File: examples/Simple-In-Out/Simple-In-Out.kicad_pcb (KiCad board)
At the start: 2 copper layers, 2 parts, among them J1 IN, J2 OUT

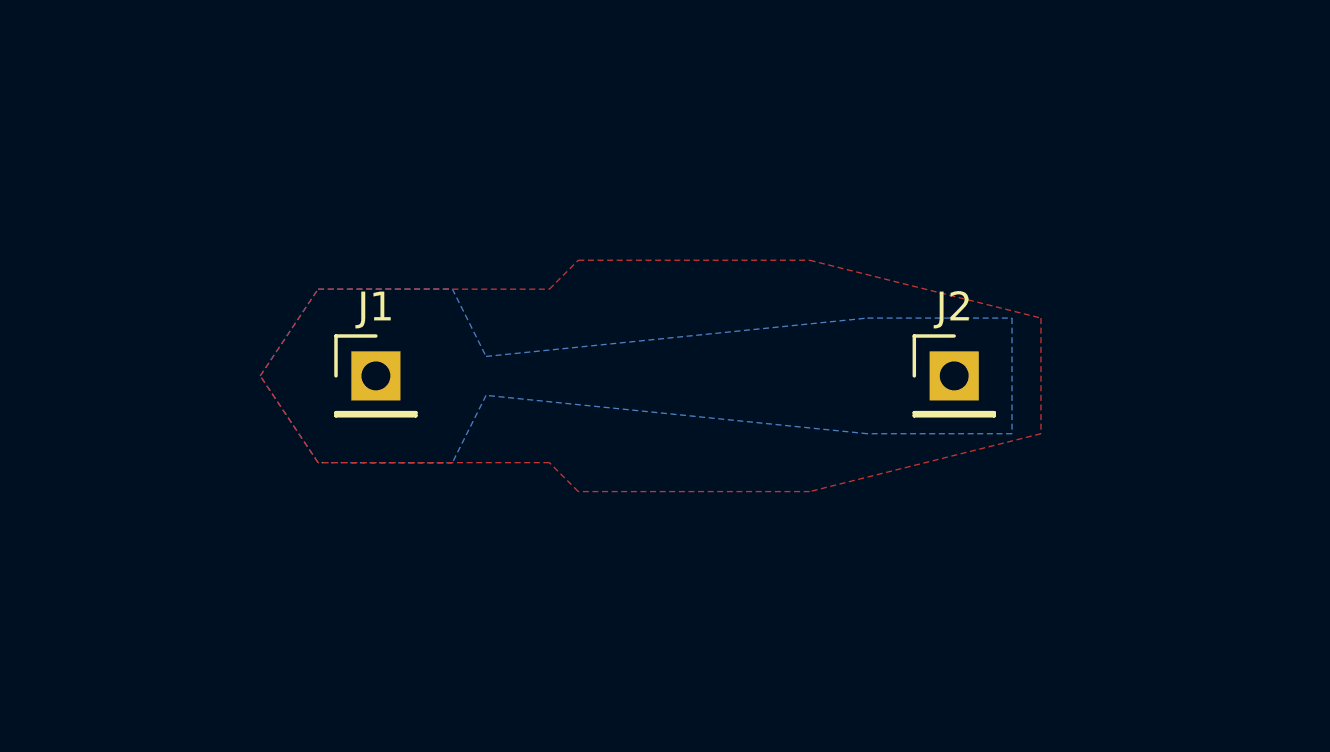
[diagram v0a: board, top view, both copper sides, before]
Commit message: Fix edge cuts
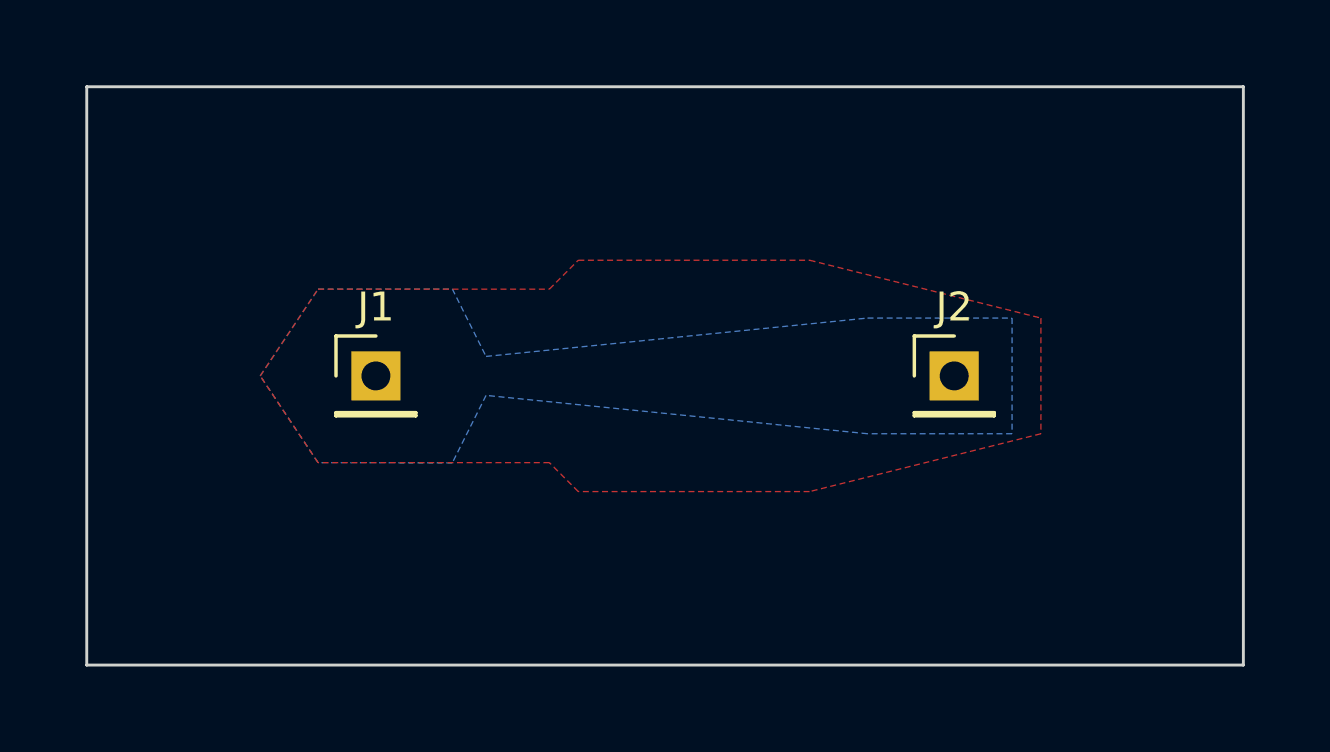
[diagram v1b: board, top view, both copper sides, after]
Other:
- board outline added: 40 x 20 mm
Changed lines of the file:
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@@
 		)
 		(fill no)
-		(layer "Eco2.User")
+		(layer "Edge.Cuts")
 	)
 	(zone

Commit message: Add GND net and vias
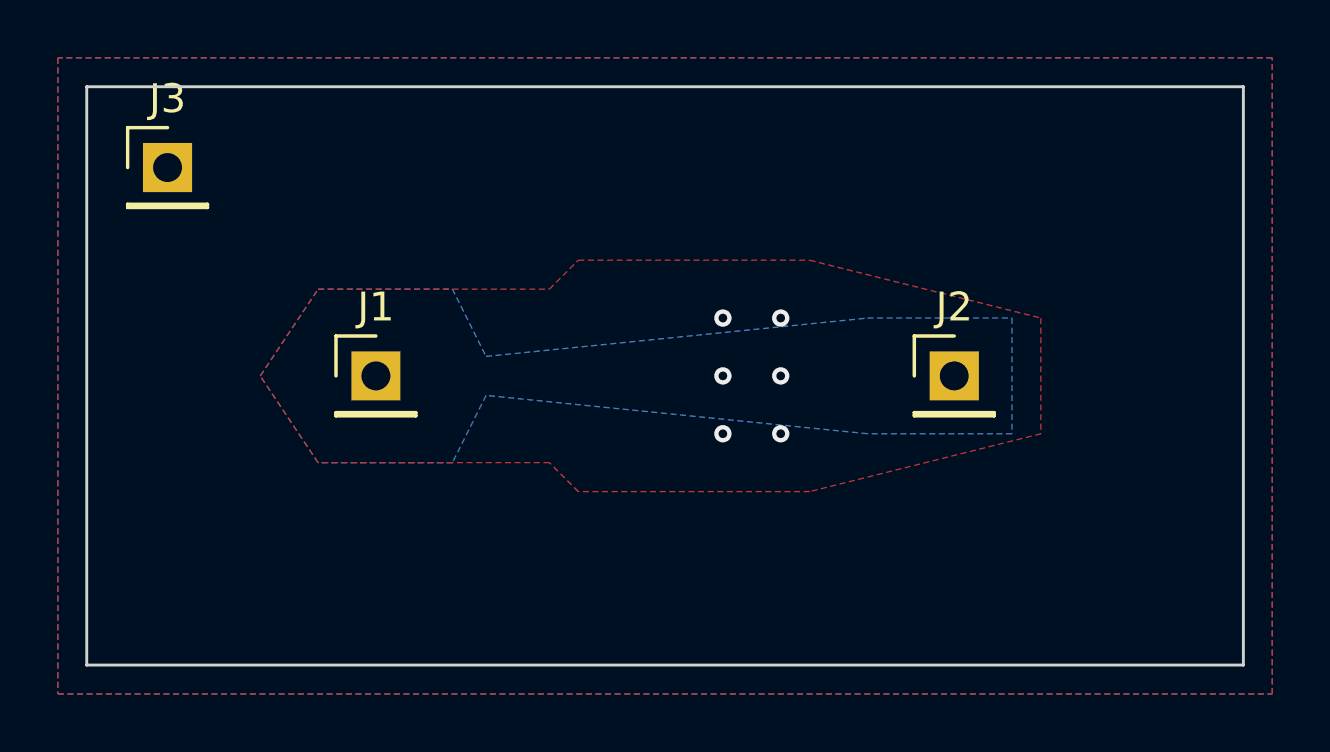
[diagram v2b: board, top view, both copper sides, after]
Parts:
- added J3: GND, Connector_PinHeader_2.54mm:PinHeader_1x01_P2.54mm_Vertical, F.Cu at (82.8, 62.8)
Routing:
- net /NET: vias 0 -> 6
- added copper zone on B.Cu, net GND
- added copper zone on F.Cu, net GND
